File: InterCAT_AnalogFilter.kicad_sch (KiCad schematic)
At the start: 42 parts

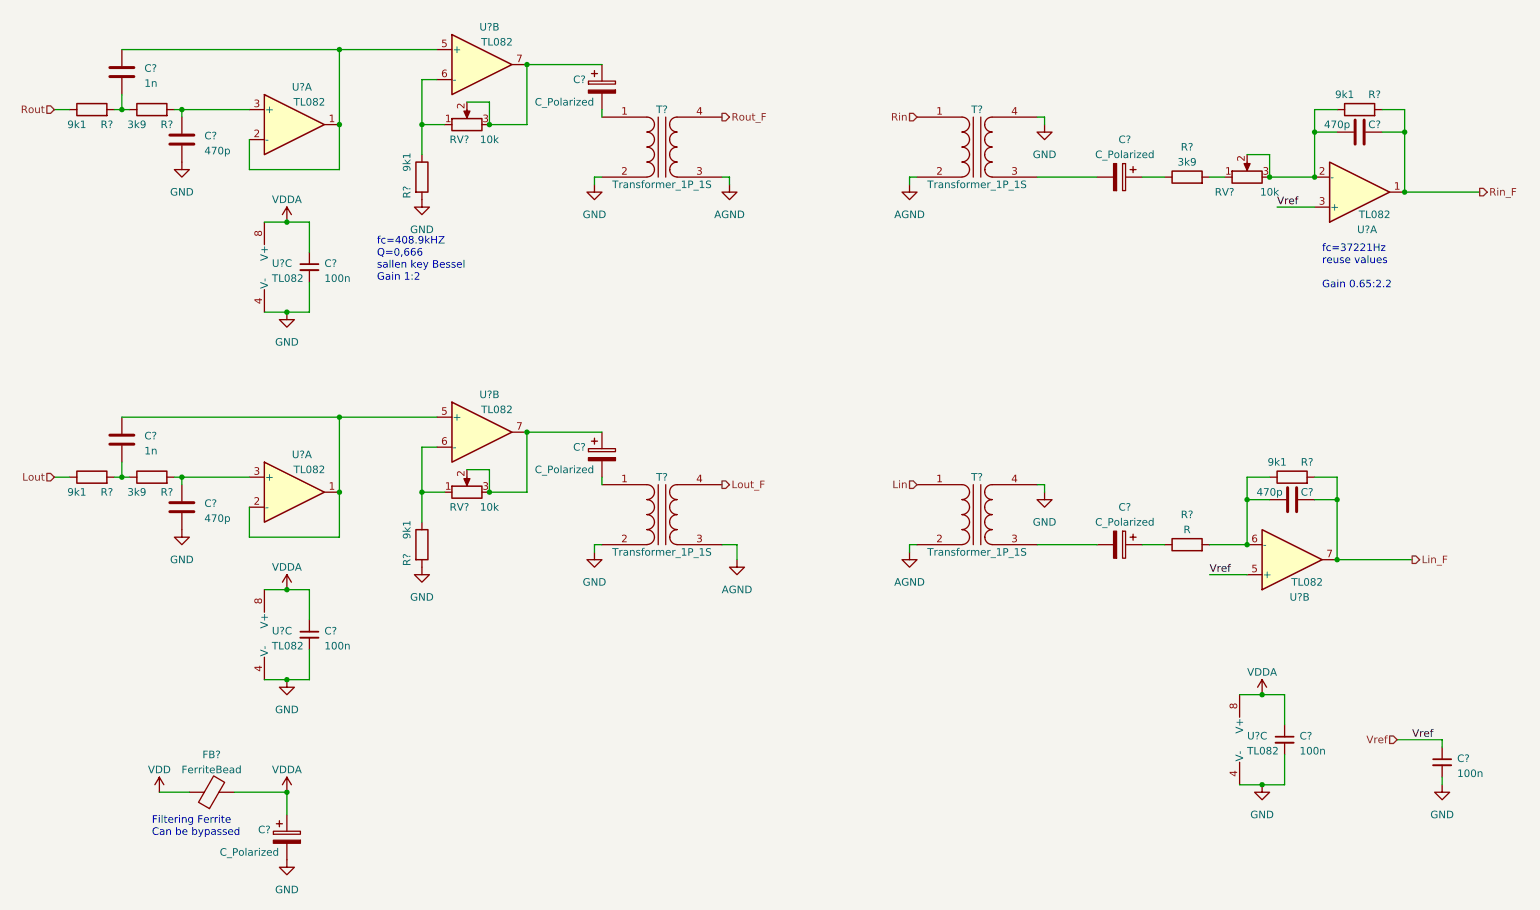
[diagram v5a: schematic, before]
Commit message: Started working on the PCB. alignement in analog channels. changed opamps ot Microchip RRIO basic on LCSC updated footprint on maxim Added LCSC parameter corrected some errors in GND/AGND corrected some errors in VCCA/VCC
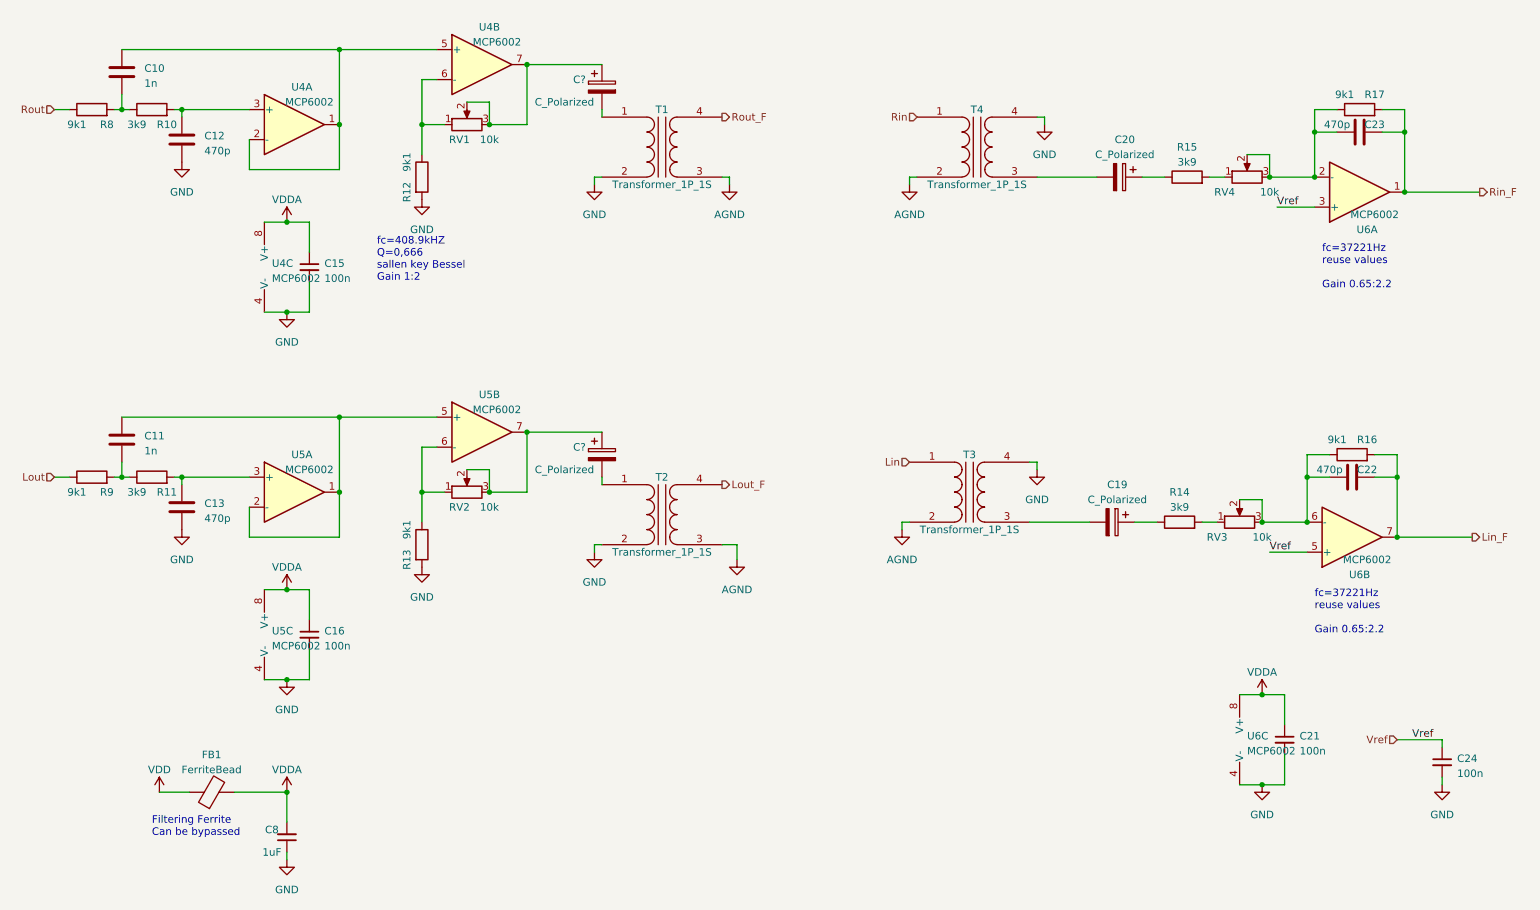
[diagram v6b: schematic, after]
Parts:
- removed C? (x2): C_Polarized, symbol Device:C_Polarized
- removed C?: 470p, symbol Device:C
- removed R?: R, symbol Device:R
- removed R?: 9k1, symbol Device:R
- removed T?: Transformer_1P_1S, symbol Device:Transformer_1P_1S
- removed U?: TL082, symbol Amplifier_Operational:TL082
- added C19: C_Polarized, Capacitor_THT:CP_Radial_D5.0mm_P2.50mm, symbol Device:C_Polarized
- added C22: 470p, Capacitor_SMD:C_0603_1608Metric, symbol Device:C
- added C8: 1uF, Capacitor_SMD:C_0603_1608Metric, symbol Device:C_Small
- added R14: 3k9, Resistor_SMD:R_0603_1608Metric, symbol Device:R
- added R16: 9k1, Resistor_SMD:R_0603_1608Metric, symbol Device:R
- added RV3: 10k, symbol Device:R_Potentiometer
- added T3: Transformer_1P_1S, symbol Device:Transformer_1P_1S
- added unit 2 of U6
- C10, C11, C12, C13, C15, C16, C21, C23, C24: renamed from C?; footprint (none) -> Capacitor_SMD:C_0603_1608Metric
- C20: renamed from C?; footprint (none) -> Capacitor_THT:CP_Radial_D5.0mm_P2.50mm
- C? (x2): footprint (none) -> Capacitor_THT:CP_Radial_D5.0mm_P2.50mm
- FB1: renamed from FB?; footprint (none) -> Resistor_SMD:R_0603_1608Metric
- R10, R11, R12, R13, R15, R17, R8, R9: renamed from R?; footprint (none) -> Resistor_SMD:R_0603_1608Metric
- U4, U5, U6: renamed from U?; value TL082 -> MCP6002; footprint (none) -> Package_SO:SOIC-8_3.9x4.9mm_P1.27mm
- gave numbers to parts that had none: 6
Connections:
- net GND: now also C8.1, T3.2 (AB), T3.4 (SB)
- net Lin: now also T3.1 (AA)
- net Lin_F: now also C22.2, R16.2, U6.7
- net VDD: no longer C15.1, C21.1, FB1.2, U4.8 (V+), U6.8 (V+)
- net Vref: now also U6.5 (+)
- new net: C22.1, R16.1, RV3.2, RV3.3, U6.6 (-)
- new net: C19.1, R14.1
- new net: R14.2, RV3.1
- new net: C19.2, T3.3 (SA)
- new net VDDA: C15.1, C21.1, C8.2, FB1.2, U4.8 (V+), U6.8 (V+)

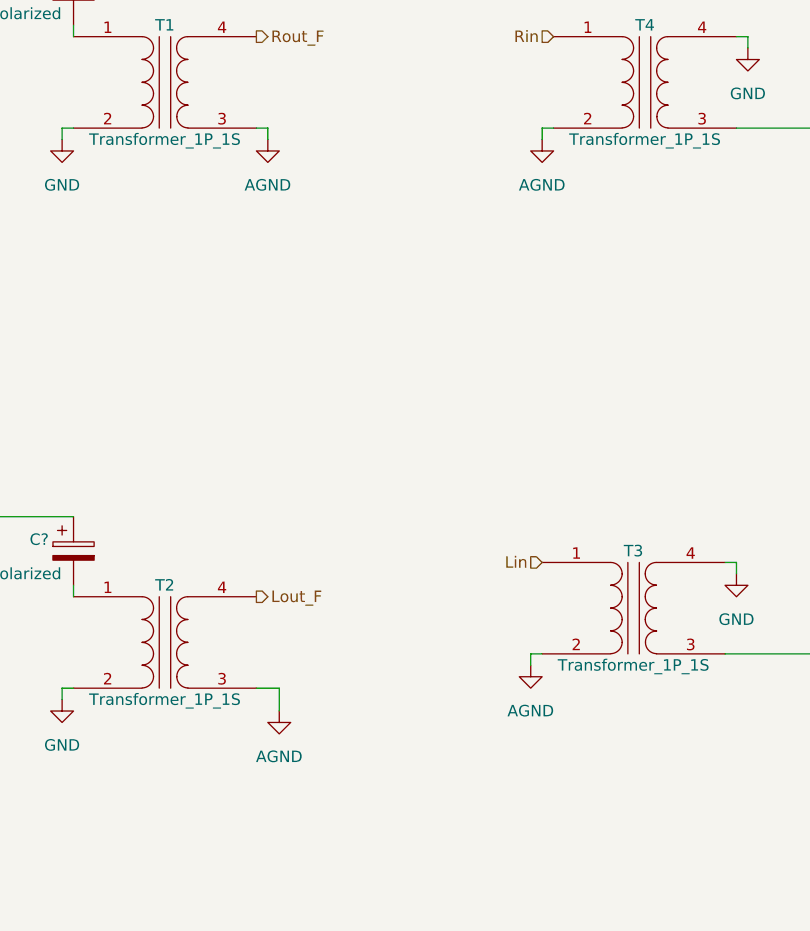
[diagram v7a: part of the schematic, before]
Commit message: Corrected hidden errors in power nets naming
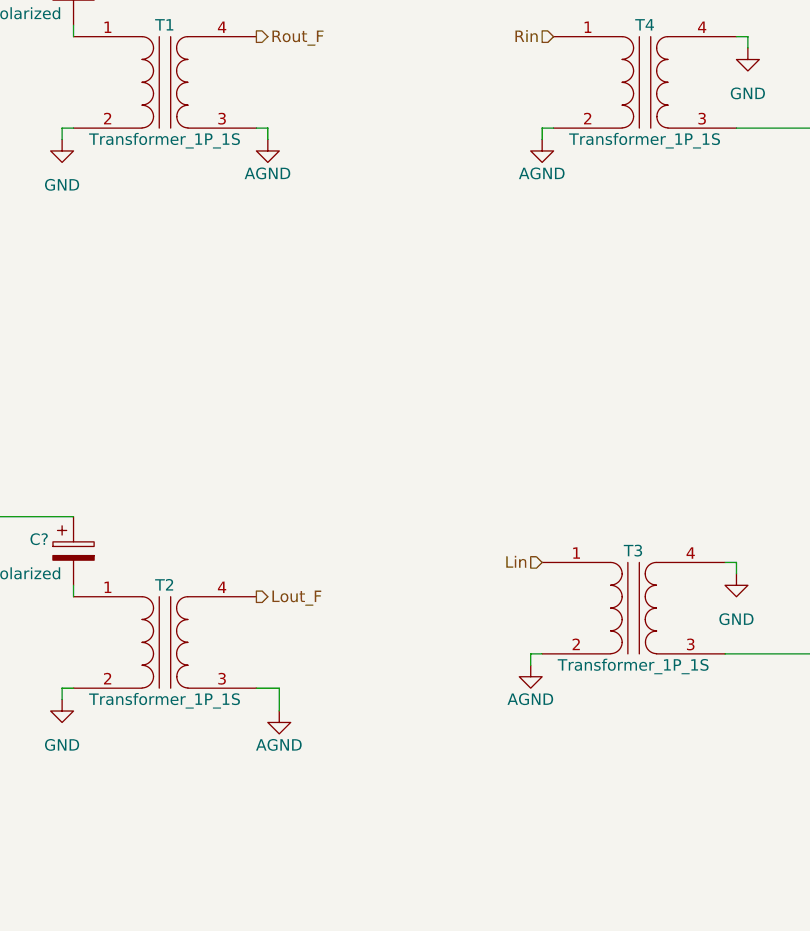
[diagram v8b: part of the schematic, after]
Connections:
- net GND: no longer T1.3 (SA), T2.3 (SA), T3.2 (AB), T4.2 (AB)
- new net GNDA: T1.3 (SA), T2.3 (SA), T3.2 (AB), T4.2 (AB)
